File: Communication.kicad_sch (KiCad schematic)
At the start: 43 parts, among them CN2 POGOPIN_2X04_P2.54_M, U1 STM32L476RGT6, U11 BUTTON, U12 32.768kHz, U13 30MHz, U14 CR1220THM, U15 100nH, U16 BMI270, U2 MPL3115A2, U4 LIS3DHTR_C15134, U5 MAX-M10S-00B-01

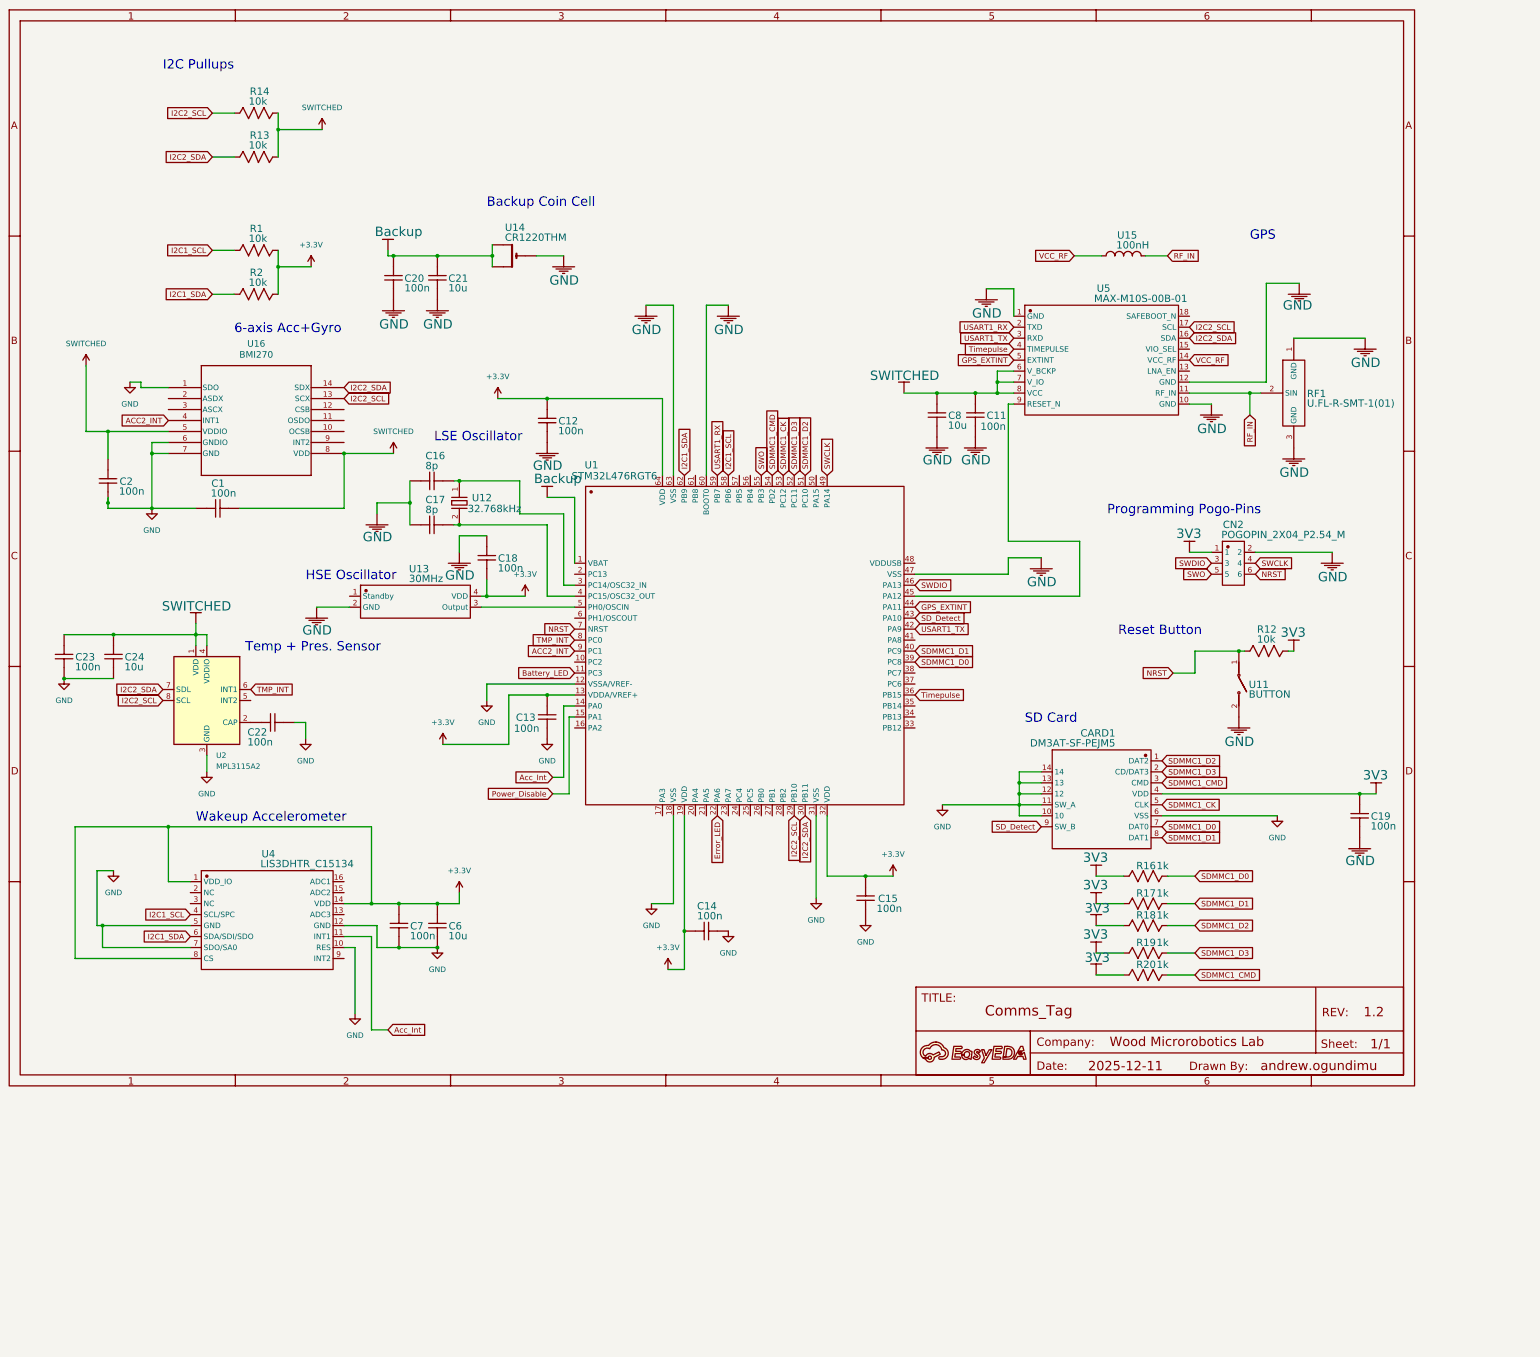
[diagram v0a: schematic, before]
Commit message: replaced MCU
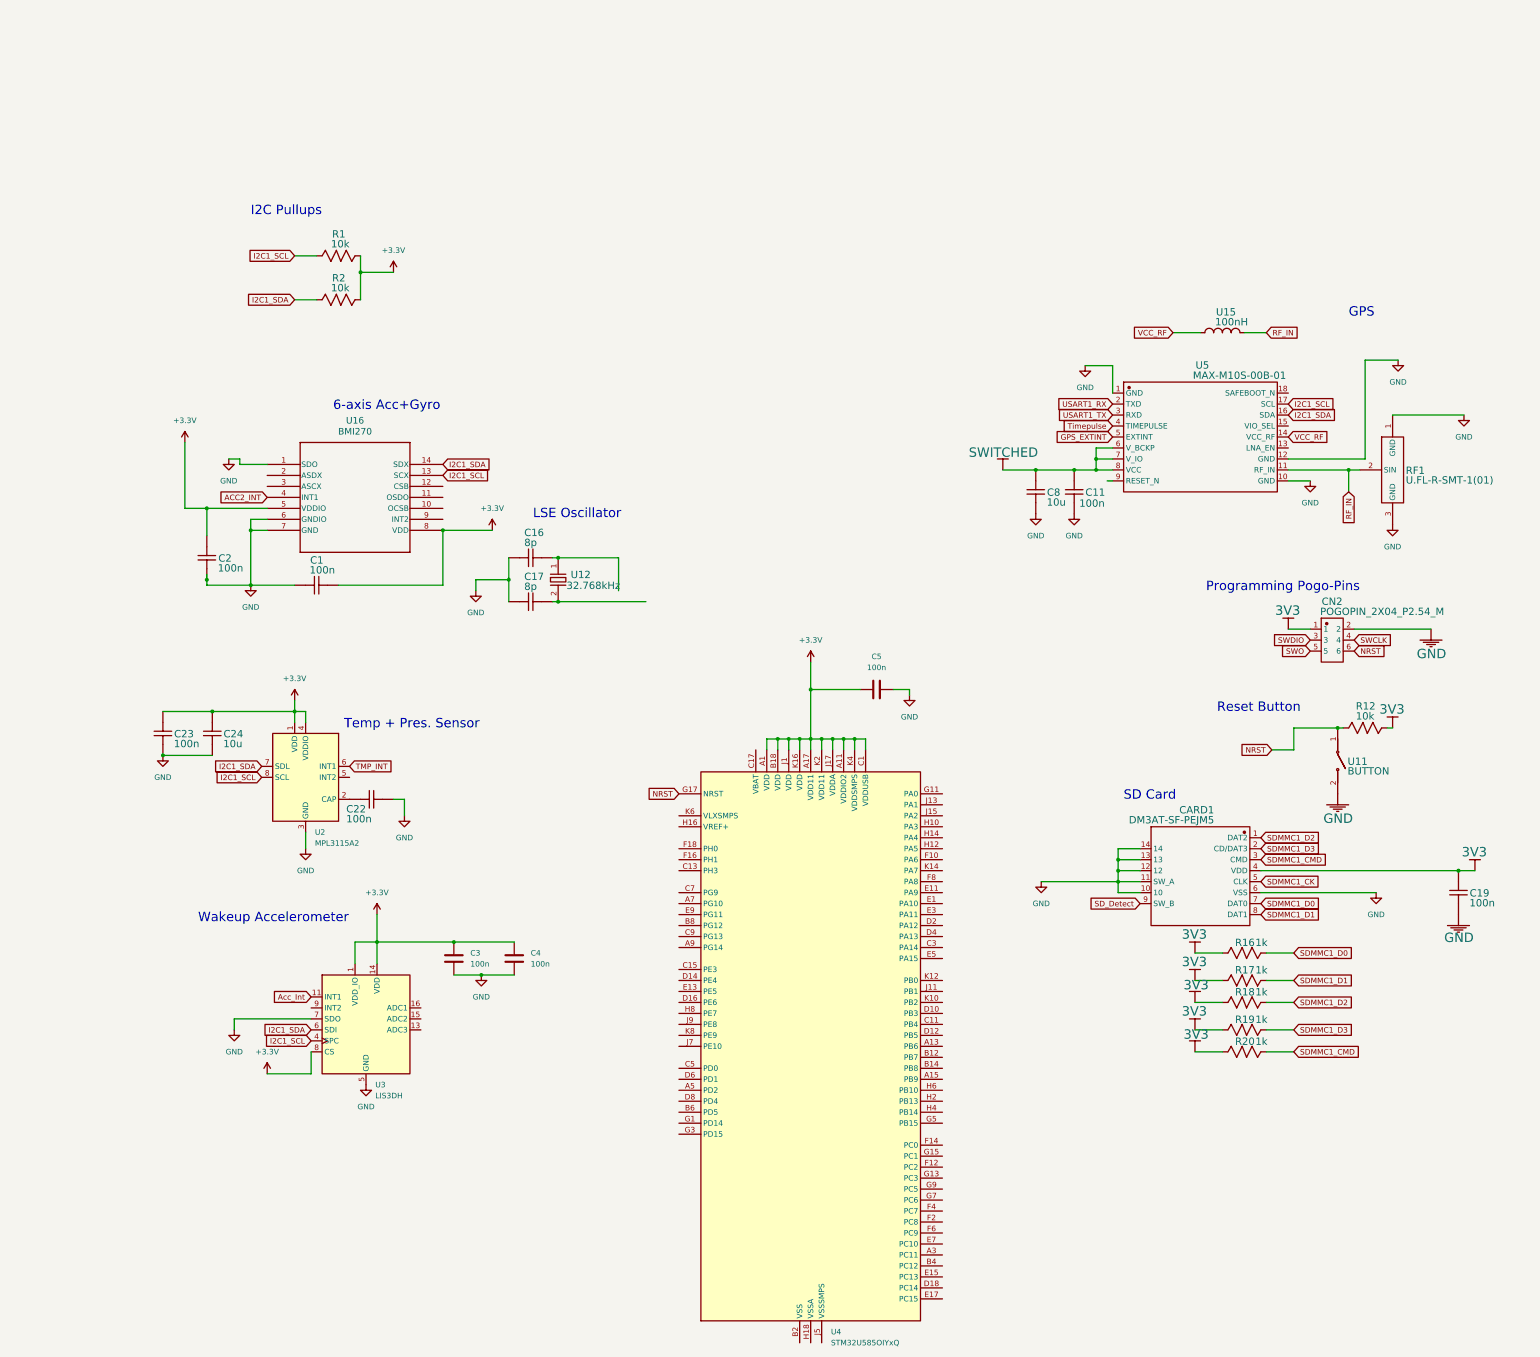
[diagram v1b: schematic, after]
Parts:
- removed A: A, symbol Unknown_-60_-984
- removed C12: 100n, symbol C_0603_US_9
- removed C13: 100n, symbol C_0603_US_10
- removed C14: 100n, symbol C_0603_US_11
- removed C15: 100n, symbol C_0603_US_12
- removed C18: 100n, symbol C_0603_US_15
- removed C20: 100n, symbol C_0603_US_17
- removed C21: 10u, symbol C_0603_US_18
- removed C6: 10u, symbol C_0603_US_5
- removed C7: 100n, symbol C_0603_US_6
- removed R13: 10k, symbol R_0603_US_3
- removed R14: 10k, symbol R_0603_US_4
- removed U1: STM32L476RGT6, symbol STM32L476RGT6
- removed U13: 30MHz, symbol ASDMB-30.000MHZ-XY-T
- removed U14: CR1220THM, symbol CR1220THM
- removed U4: LIS3DHTR_C15134, symbol LIS3DHTR_C15134
- added C3, C4, C5: 100n, symbol Device:C
- added U3: LIS3DH, Package_LGA:LGA-16_3x3mm_P0.5mm_LayoutBorder3x5y, symbol Sensor_Motion:LIS3DH
- added U4: STM32U585OIYxQ, Package_CSP:ST_WLCSP-90_4.2x3.95mm_Layout18x10_P0.4mm_Stagger, symbol MCU_ST_STM32U5:STM32U585OIYxQ
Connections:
- net I2C2_SCL is gone; now on net I2C1_SCL: U16.13 (SCX), U2.8 (SCL), U5.17 (SCL)
- net I2C2_SDA is gone; now on net I2C1_SDA: U16.14 (SDX), U2.7 (SDL), U5.16 (SDA)
- net +3.3V: now also C1.2, C2.2, C23.2, C24.2, U16.5 (VDDIO), U16.8 (VDD), U2.1 (VDD), U2.4 (VDDIO), C3.1, C4.1, C5.1, U3.1 (VDD_IO), U3.14 (VDD), U3.8 (CS), U4.A1 (VDD), U4.A11 (VDDIO2), U4.A17 (VDD11), U4.B18 (VDD), U4.C1 (VDDUSB), U4.J1 (VDD), U4.J17 (VDDA), U4.K16 (VDD), U4.K2 (VDD11), U4.K4 (VDDSMPS)
- net Acc_Int: now also U3.11 (INT1)
- net GND: now also C3.2, C4.2, C5.2, U3.10 (GND), U3.12 (GND), U3.5 (GND), U3.7 (SDO)
- net I2C1_SCL: now also U3.4 (SPC)
- net I2C1_SDA: now also U3.6 (SDI)
- net NRST: now also U4.G17 (NRST)
- net SWITCHED: no longer C1.2, C2.2, C23.2, C24.2, U16.5 (VDDIO), U16.8 (VDD), U2.1 (VDD), U2.4 (VDDIO)
- new net: U4.B10 (VSS), U4.B16 (VSS), U4.B2 (VSS), U4.J3 (VSS), U4.K18 (VSS)
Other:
- note removed: "Backup Coin Cell"
- note removed: "HSE Oscillator"
- moved on the sheet: C1, C11, C16, C17, C19, C2, C22, C23, C24, C8, CARD1, CN2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
